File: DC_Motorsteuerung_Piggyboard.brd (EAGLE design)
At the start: 35.2 x 100 mm, 18 parts

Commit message: Piggiboard updated (ERROR LED)
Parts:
- removed R4: 160R, Resistor:R_0,4W
- removed R8: 90R, Resistor:R_0,4W
- D6: value (none) -> Error; device LED:RGBLED5MM -> Test:LED3MMCASE
- R7: value 90R -> 1,5k
- moved D6 6.99 mm to (0.00, 43.8)
- moved R7 3.81 mm to (14.6, 45.1)
- moved D1 0.63 mm to (0.00, 53.7)
- moved R3 0.63 mm to (14.6, 54.9)
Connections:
- removed net N$16: R4.1, SV2.6
- removed net N$17: D6.P$4, R7.2
- removed net N$18: D6.P$1, R8.2
- removed net N$19: D6.P$2, R4.2
- net GND: now also D6.P$2; no longer D6.P$3
- net N$5: now also D6.P$1, R7.2; no longer R8.1, SV2.4
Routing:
- net N$16: track 39.6 -> 0.00 mm
- net N$19: track 15.7 -> 0.00 mm
- net N$5: track 18.8 -> 5.22 mm
- net N$18: track 8.15 -> 0.00 mm
- net N$17: track 6.61 -> 0.00 mm
- net N$15: track 24.3 -> 20.5 mm
- net N$6: track 19.9 -> 20.5 mm
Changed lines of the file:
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@@
 </autorouter>
 <elements>
-<element name="D1" library="Test" package="LED3MMCASE" value="+24V" x="0" y="54.2925"/>
+<element name="D1" library="Test" package="LED3MMCASE" value="+24V" x="0" y="53.6575"/>
 <element name="D2" library="Test" package="LED3MMCASE" value="Moves A" x="0" y="34.29"/>
 <element name="D3" library="Test" package="LED3MMCASE" value="Limit A" x="0" y="24.765"/>
@@
 <attribute name="VALUE" x="19.05" y="10.4775" size="1.778" layer="27" rot="R180"/>
 </element>
-<element name="R3" library="Resistor" package="R_0,4W" value="1,5k" x="14.605" y="55.5625" smashed="yes" rot="R180">
-<attribute name="NAME" x="20.32" y="55.5625" size="1.778" layer="25"/>
-<attribute name="VALUE" x="19.05" y="59.055" size="1.778" layer="27" rot="R180"/>
+<element name="R3" library="Resistor" package="R_0,4W" value="1,5k" x="14.605" y="54.9275" smashed="yes" rot="R180">
+<attribute name="NAME" x="20.32" y="54.9275" size="1.778" layer="25"/>
+<attribute name="VALUE" x="19.05" y="58.42" size="1.778" layer="27" rot="R180"/>
 </element>
 <element name="R5" library="Resistor" package="R_0,4W" value="1,5k" x="14.605" y="35.56" smashed="yes" rot="R180">
@@
 <element name="H1" library="Holes" package="3,2" value="Das Loch 3,2 kilometer" x="25.4" y="46.355"/>
 <element name="U$2" library="Test" package="UMSCHALTER_SINGLE_POLE" value="UMSCHALTER_SINGLE_POLE" x="12.7" y="90.17"/>
-<element name="D6" library="LED" package="RGBLED5MM" value="" x="6.985" y="43.815"/>
 <element name="SV2" library="con-lstb" package="MA06-2" value="" x="24.765" y="69.85" rot="R90">
 <attribute name="OC_NEWARK" value="unknown" x="24.765" y="69.85" size="0.066" layer="27" font="vector" ratio="15" rot="R90" display="off"/>
@@
 <attribute name="OC_FARNELL" value="unknown" x="24.765" y="69.85" size="0.066" layer="27" font="vector" ratio="15" rot="R90" display="off"/>
 </element>
-<element name="R4" library="Resistor" package="R_0,4W" value="160R" x="14.605" y="38.735" smashed="yes" rot="R180">
-<attribute name="NAME" x="20.32" y="38.4175" size="1.778" layer="25"/>
-<attribute name="VALUE" x="22.225" y="33.3375" size="1.778" layer="27"/>
+<element name="R7" library="Resistor" package="R_0,4W" value="1,5k" x="14.605" y="45.085" smashed="yes" rot="R180">
+<attribute name="NAME" x="20.32" y="44.7675" size="1.778" layer="25"/>
+<attribute name="VALUE" x="19.05" y="48.5775" size="1.778" layer="27" rot="R180"/>
 </element>
-<element name="R8" library="Resistor" package="R_0,4W" value="90R" x="14.605" y="50.8" smashed="yes" rot="R180">
-<attribute name="NAME" x="20.32" y="50.8" size="1.778" layer="25"/>
-<attribute name="VALUE" x="8.89" y="52.3875" size="1.778" layer="27"/>
-</element>
-<element name="R7" library="Resistor" package="R_0,4W" value="90R" x="14.605" y="41.275" smashed="yes" rot="R180">
-<attribute name="NAME" x="20.32" y="40.9575" size="1.778" layer="25"/>
-<attribute name="VALUE" x="19.05" y="44.7675" size="1.778" layer="27" rot="R180"/>
-</element>
+<element name="D6" library="Test" package="LED3MMCASE" value="Error" x="0" y="43.815"/>
 </elements>
 <signals>
@@
 </polygon>
 <contactref element="U$2" pad="P$2"/>
-<contactref element="D6" pad="P$3"/>
 <contactref element="SV2" pad="11"/>
+<contactref element="D6" pad="P$2"/>
 </signal>
 <signal name="N$12">
@@
 <contactref element="R3" pad="1"/>
 <contactref element="SV2" pad="8"/>
-<wire x1="18.415" y1="55.5625" x2="18.415" y2="69.85" width="0.6096" layer="16"/>
+<wire x1="18.415" y1="54.9275" x2="18.415" y2="69.85" width="0.6096" layer="16"/>
 <wire x1="18.415" y1="69.85" x2="19.685" y2="71.12" width="0.6096" layer="16"/>
 <wire x1="19.685" y1="71.12" x2="23.495" y2="71.12" width="0.6096" layer="16"/>
@@
 <contactref element="D1" pad="P$1"/>
 <contactref element="R3" pad="2"/>
-<wire x1="6.84" y1="55.5625" x2="12.065" y2="55.5625" width="0.6096" layer="16"/>
+<wire x1="6.84" y1="54.9275" x2="12.065" y2="54.9275" width="0.6096" layer="16"/>
 </signal>
 <signal name="N$1">
@@
 <wire x1="6.84" y1="35.56" x2="12.065" y2="35.56" width="0.6096" layer="16"/>
 </signal>
-<signal name="N$5">
-<contactref element="R8" pad="1"/>
-<contactref element="SV2" pad="4"/>
-<wire x1="18.415" y1="50.8" x2="20.32" y2="50.8" width="0.6096" layer="16"/>
-<wire x1="20.32" y1="50.8" x2="21.59" y2="52.07" width="0.6096" layer="16"/>
-<wire x1="21.59" y1="52.07" x2="21.59" y2="64.77" width="0.6096" layer="16"/>
-<wire x1="21.59" y1="64.77" x2="22.86" y2="66.04" width="0.6096" layer="16"/>
-<wire x1="22.86" y1="66.04" x2="23.495" y2="66.04" width="0.6096" layer="16"/>
-</signal>
 <signal name="N$15">
 <contactref element="R7" pad="1"/>
 <contactref element="SV2" pad="2"/>
-<wire x1="18.415" y1="41.275" x2="18.415" y2="46.355" width="0.6096" layer="16"/>
-<wire x1="18.415" y1="46.355" x2="19.685" y2="47.625" width="0.6096" layer="16"/>
-<wire x1="19.685" y1="47.625" x2="21.59" y2="49.53" width="0.6096" layer="16"/>
-<wire x1="21.59" y1="49.53" x2="22.86" y2="50.8" width="0.6096" layer="16"/>
-<wire x1="22.86" y1="50.8" x2="23.495" y2="51.435" width="0.6096" layer="16"/>
-<wire x1="23.495" y1="51.435" x2="23.495" y2="63.5" width="0.6096" layer="16"/>
-</signal>
-<signal name="N$16">
-<contactref element="R4" pad="1"/>
-<contactref element="SV2" pad="6"/>
-<wire x1="18.415" y1="38.735" x2="15.875" y2="38.735" width="0.6096" layer="16"/>
-<wire x1="15.875" y1="38.735" x2="14.605" y2="40.005" width="0.6096" layer="16"/>
-<wire x1="14.605" y1="40.005" x2="14.605" y2="51.435" width="0.6096" layer="16"/>
-<wire x1="14.605" y1="51.435" x2="15.875" y2="52.705" width="0.6096" layer="16"/>
-<wire x1="15.875" y1="52.705" x2="19.05" y2="52.705" width="0.6096" layer="16"/>
-<wire x1="19.05" y1="52.705" x2="20.32" y2="53.975" width="0.6096" layer="16"/>
-<wire x1="20.32" y1="53.975" x2="20.32" y2="67.31" width="0.6096" layer="16"/>
-<wire x1="20.32" y1="67.31" x2="21.59" y2="68.58" width="0.6096" layer="16"/>
-<wire x1="21.59" y1="68.58" x2="23.495" y2="68.58" width="0.6096" layer="16"/>
-</signal>
-<signal name="N$17">
-<contactref element="R7" pad="2"/>
-<contactref element="D6" pad="P$4"/>
-<wire x1="5.715" y1="41.91" x2="6.35" y2="41.275" width="0.6096" layer="16"/>
-<wire x1="6.35" y1="41.275" x2="12.065" y2="41.275" width="0.6096" layer="16"/>
-</signal>
-<signal name="N$18">
-<contactref element="R8" pad="2"/>
-<contactref element="D6" pad="P$1"/>
-<wire x1="8.255" y1="45.72" x2="8.255" y2="49.53" width="0.6096" layer="16"/>
-<wire x1="8.255" y1="49.53" x2="9.525" y2="50.8" width="0.6096" layer="16"/>
-<wire x1="9.525" y1="50.8" x2="12.065" y2="50.8" width="0.6096" layer="16"/>
-</signal>
-<signal name="N$19">
-<contactref element="R4" pad="2"/>
-<contactref element="D6" pad="P$2"/>
-<wire x1="5.715" y1="44.45" x2="4.445" y2="44.45" width="0.6096" layer="16"/>
-<wire x1="4.445" y1="44.45" x2="3.175" y2="43.18" width="0.6096" layer="16"/>
-<wire x1="3.175" y1="43.18" x2="3.175" y2="40.005" width="0.6096" layer="16"/>
-<wire x1="3.175" y1="40.005" x2="4.445" y2="38.735" width="0.6096" layer="16"/>
-<wire x1="4.445" y1="38.735" x2="12.065" y2="38.735" width="0.6096" layer="16"/>
+<wire x1="18.415" y1="45.085" x2="18.415" y2="47.625" width="0.6096" layer="16"/>
+<wire x1="18.415" y1="47.625" x2="23.495" y2="52.705" width="0.6096" layer="16"/>
+<wire x1="23.495" y1="52.705" x2="23.495" y2="63.5" width="0.6096" layer="16"/>
 </signal>
 <signal name="N$20">
@@
 <wire x1="11.357" y1="76.2" x2="11.357" y2="76.194" width="0.4064" layer="16"/>
 </signal>
+<signal name="N$5">
+<contactref element="R7" pad="2"/>
+<contactref element="D6" pad="P$1"/>
+<wire x1="12.065" y1="45.085" x2="6.84" y2="45.085" width="0.6096" layer="16"/>
+</signal>
 </signals>

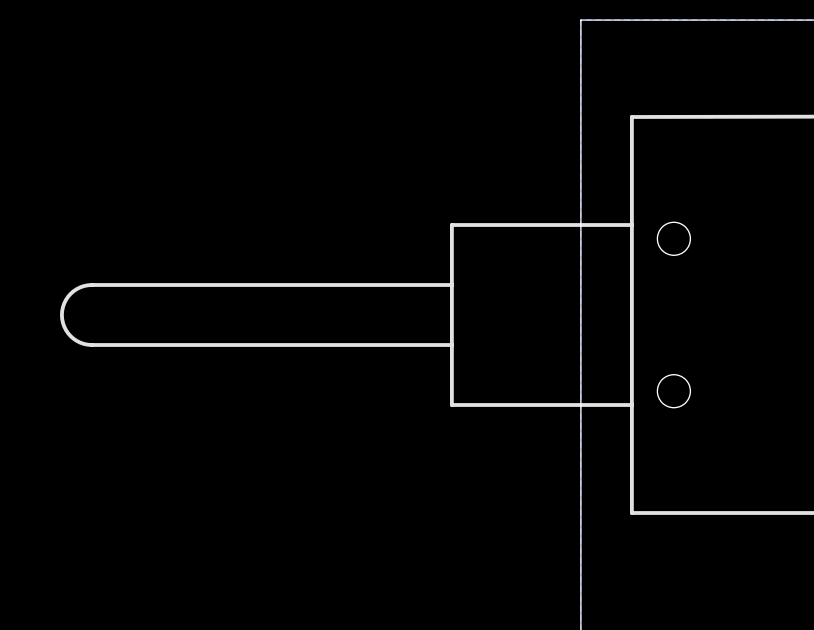
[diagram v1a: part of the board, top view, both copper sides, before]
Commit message: Piggyboard & Board updated
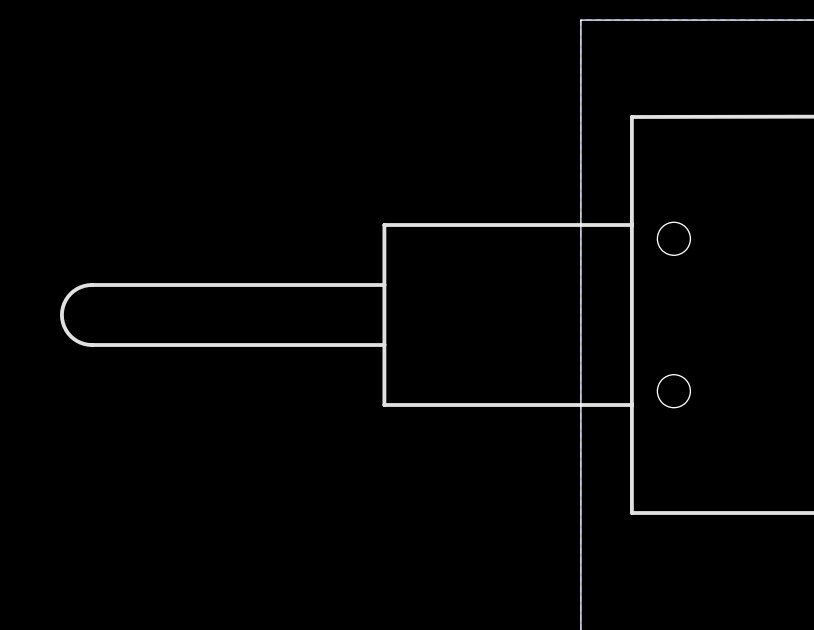
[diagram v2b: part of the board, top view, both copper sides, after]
